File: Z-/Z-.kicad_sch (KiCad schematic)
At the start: 27 parts, among them J1 200528-0100, J2 U.FL, J3 U.FL, J5 Conn_01x02, U5 USBLC6-2P6

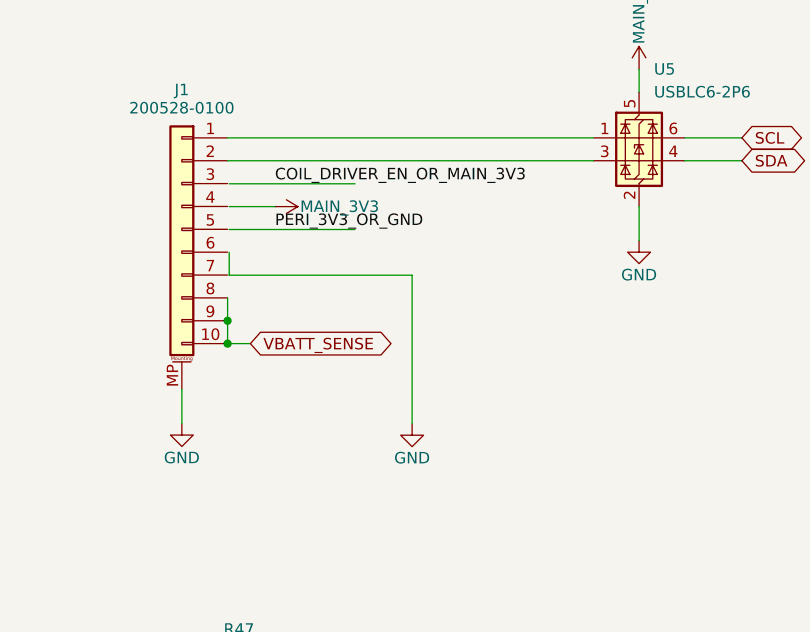
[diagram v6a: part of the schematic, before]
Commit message: Updated schematics/layout with mainboard compatability
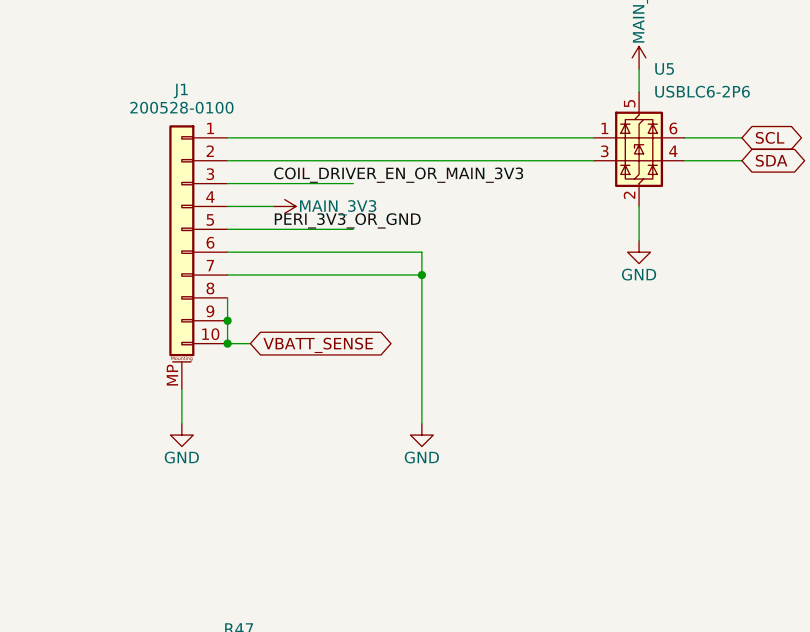
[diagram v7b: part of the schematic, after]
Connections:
- net COIL_DRIVER_EN_OR_MAIN_3V3: now also J1.3 (Pin_3)
- net GND: now also J1.6 (Pin_6), J1.7 (Pin_7)
- net MAIN_3V3: now also J1.4 (Pin_4)
- net PERI_3V3_OR_GND: now also J1.5 (Pin_5)
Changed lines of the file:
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@@
+	)
+	(junction
+		(at 85.09 123.19)
+		(diameter 0)
+		(color 0 0 0 0)
 	)
 	(junction
@@
 	(wire
 		(pts
-			(xy 68.7632 115.5885) (xy 63.6832 115.5885)
-		)
-		(stroke
-			(width 0)
-			(type default)
-		)
-	)
-	(wire
-		(pts
 			(xy 151.13 172.72) (xy 151.13 177.8)
 		)
@@
 	(wire
 		(pts
+			(xy 85.09 120.65) (xy 85.09 123.19)
+		)
+		(stroke
+			(width 0)
+			(type default)
+		)
+	)
+	(wire
+		(pts
 			(xy 252.73 128.27) (xy 252.73 130.81)
 		)
@@
 	(wire
 		(pts
-			(xy 84.0032 139.7185) (xy 84.0032 123.2085)
-		)
-		(stroke
-			(width 0)
-			(type default)
-		)
-	)
-	(wire
-		(pts
-			(xy 63.6832 118.1285) (xy 77.6532 118.1285)
+			(xy 63.5 120.65) (xy 85.09 120.65)
 		)
 		(stroke
@@
 	(wire
 		(pts
+			(xy 63.5 118.11) (xy 77.47 118.11)
+		)
+		(stroke
+			(width 0)
+			(type default)
+		)
+	)
+	(wire
+		(pts
 			(xy 252.73 138.43) (xy 252.73 140.97)
 		)
@@
 	(wire
 		(pts
+			(xy 68.58 115.57) (xy 63.5 115.57)
+		)
+		(stroke
+			(width 0)
+			(type default)
+		)
+	)
+	(wire
+		(pts
 			(xy 69.85 177.8) (xy 67.31 177.8)
 		)
@@
 	(wire
 		(pts
+			(xy 85.09 139.7) (xy 85.09 123.19)
+		)
+		(stroke
+			(width 0)
+			(type default)
+		)
+	)
+	(wire
+		(pts
 			(xy 205.74 128.27) (xy 229.87 128.27)
 		)
@@
 	(wire
 		(pts
-			(xy 63.6832 123.2085) (xy 84.0032 123.2085)
+			(xy 63.5 123.19) (xy 85.09 123.19)
 		)
 		(stroke
@@
 	(wire
 		(pts
-			(xy 63.6832 113.0485) (xy 77.6532 113.0485)
-		)
-		(stroke
-			(width 0)
-			(type default)
-		)
-	)
-	(wire
-		(pts
 			(xy 64.77 38.1) (xy 69.85 38.1)
 		)
@@
 	(wire
 		(pts
-			(xy 63.6832 120.6685) (xy 63.6832 123.2085)
+			(xy 63.5 113.03) (xy 77.47 113.03)
 		)
 		(stroke
@@
 		)
 	)
-	(label "COIL_DRIVER_EN_OR_MAIN_3V3"
-		(at 68.7632 113.0485 0)
+	(label "PERI_3V3_OR_GND"
+		(at 68.58 118.11 0)
 		(fields_autoplaced yes)
 		(effects
@@
 		)
 	)
-	(label "PERI_3V3_OR_GND"
-		(at 68.7632 118.1285 0)
+	(label "COIL_DRIVER_EN_OR_MAIN_3V3"
+		(at 68.58 113.03 0)
 		(fields_autoplaced yes)
 		(effects
@@
 	)
 	(symbol
-		(lib_id "power:+3.3V")
-		(at 68.7632 115.5885 270)
-		(mirror x)
-		(unit 1)
-		(exclude_from_sim no)
-		(in_bom yes)
-		(on_board yes)
-		(dnp no)
-		(property "Reference" "#SUPPLY01"
-			(at 68.7632 115.5885 0)
-			(effects
-				(font
-					(size 1.27 1.27)
-				)
-				(hide yes)
-			)
-		)
-		(property "Value" "MAIN_3V3"
-			(at 71.5572 115.5885 90)
-			(effects
-				(font
-					(size 1.27 1.27)
-				)
-				(justify left)
-			)
-		)
-		(property "Footprint" ""
-			(at 68.7632 115.5885 0)
-			(effects
-				(font
-					(size 1.27 1.27)
-				)
-				(hide yes)
-			)
-		)
-		(property "Datasheet" ""
-			(at 68.7632 115.5885 0)
-			(effects
-				(font
-					(size 1.27 1.27)
-				)
-				(hide yes)
-			)
-		)
-		(property "Description" "Power symbol creates a global label with name \"+3.3V\""
-			(at 68.7632 115.5885 0)
-			(effects
-				(font
-					(size 1.27 1.27)
-				)
-				(hide yes)
-			)
-		)
-		(pin "1"
-		)
-		(instances
-			(project "Z-"
-				(path "/446ceff1-46b8-4829-b15a-92d0d6c980a6"
-					(reference "#SUPPLY01")
-					(unit 1)
-				)
-			)
-		)
-	)
-	(symbol
 		(lib_id "power:GND")
 		(at 119.38 63.5 0)
@@
 	(symbol
 		(lib_id "power:GND")
-		(at 84.0032 139.7185 0)
+		(at 85.09 139.7 0)
 		(unit 1)
 		(exclude_from_sim no)
@@
 		(dnp no)
 		(property "Reference" "#PWR07"
-			(at 84.0032 146.0685 0)
+			(at 85.09 146.05 0)
 			(effects
 				(font
@@
 		)
 		(property "Value" "GND"
-			(at 84.0032 143.5285 0)
+			(at 85.09 143.51 0)
 			(effects
 				(font
@@
 		)
 		(property "Footprint" ""
-			(at 84.0032 139.7185 0)
+			(at 85.09 139.7 0)
 			(effects
 				(font
@@
 		)
 		(property "Datasheet" ""
-			(at 84.0032 139.7185 0)
+			(at 85.09 139.7 0)
 			(effects
 				(font
@@
 		)
 		(property "Description" "Power symbol creates a global label with name \"GND\" , ground"
-			(at 84.0032 139.7185 0)
+			(at 85.09 139.7 0)
 			(effects
 				(font
@@
 					(unit 1)
 				)
+			)
+		)
+	)
+	(symbol
+		(lib_id "power:+3.3V")
+		(at 68.58 115.57 270)
+		(mirror x)
+		(unit 1)
+		(exclude_from_sim no)
+		(in_bom yes)
+		(on_board yes)
+		(dnp no)
+		(property "Reference" "#SUPPLY01"
+			(at 68.58 115.57 0)
+			(effects
+				(font
+					(size 1.27 1.27)
+				)
+				(hide yes)
+			)
+		)
+		(property "Value" "MAIN_3V3"
+			(at 71.374 115.57 90)
+			(effects
+				(font
+					(size 1.27 1.27)
+				)
+				(justify left)
+			)
+		)
+		(property "Footprint" ""
+			(at 68.58 115.57 0)
+			(effects
+				(font
+					(size 1.27 1.27)
+				)
+				(hide yes)
+			)
+		)
+		(property "Datasheet" ""
+			(at 68.58 115.57 0)
+			(effects
+				(font
+					(size 1.27 1.27)
+				)
+				(hide yes)
+			)
+		)
+		(property "Description" "Power symbol creates a global label with name \"+3.3V\""
+			(at 68.58 115.57 0)
+			(effects
+				(font
+					(size 1.27 1.27)
+				)
+				(hide yes)
+			)
+		)
+		(pin "1"
+		)
+		(instances
+			(project "Z-"
+				(path "/446ceff1-46b8-4829-b15a-92d0d6c980a6"
+					(reference "#SUPPLY01")
+					(unit 1)
+				)
